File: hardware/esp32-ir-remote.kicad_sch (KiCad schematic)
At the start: 72 parts, among them J2 USB_C_Receptacle_USB2.0_14P, J3 Qwiic_I2C, J4 GPIO_PWR, J5 EXT_IR, J6 JTAG, Q1 Q_NPN_BCE, Q2 Q_NPN_BCE, Q3 IRLML6344, Q4 2N7002, Q5 2N7002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

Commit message: Fix BOM blockers found by adversarial LCSC validation (pre-routing)
Subagent validated all 35 LCSC codes against the live catalog; findings fixed:
- BLOCKER: Q1/Q2 used Q_NPN_BCE symbol but S8050 (C2146) SOT-23 is B-E-C -
  collector/emitter were swapped on the physical part (auto-reset would not
  work). Embedded symbol pin numbers swapped -> Q_NPN_BEC, wires untouched,
  netlist nodes confirm C: pad2->3, E: pad3->2; PCB pad nets swapped to match.
- BLOCKER: SW1/SW2 carried SMD switch code C455280 (TS-1088R 4x3mm) on a THT
  6mm footprint - unassemblable. Footprint -> JLC-MCP:SW-SMD_L3.9-W3.0-P4.45
  (fetched via jlcpcb MCP, validated 2 pads, clean layers); now SMT-line
  assemblable.
- HIGH: R9-R12+R30 carried C17955 = 20 ohm, not 18 - IR drive current 10% low.
  -> C17922 (18 ohm 1206 1% 250mW, Extended accepted: power margin per
  ir-transmitter.md needs 1206/0.25W).
- HIGH: 0805 codes on 1206 footprints: R3-R8+R22 -> C17902 (10k 1206 Basic);
  R1/R2 + R13/R16-R19 -> footprints to R_0805 keeping Basic 0805 codes
  (no Basic 1206 exists for 5.1k/470R).
- HIGH: JP1 testpoint (0.8mm drills) had pin-header code C124375 that cannot
  fit - code removed; JP1 is a solder-bridge/test-point, no part.
- Noted for order time: AM2302 stock critically low (37 units).

Verified: ERC 0 errors; netlist partition PCB==schematic identical;
footprint/value match 72/72; courtyard overlaps 0. BOM CSV regenerated.
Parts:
- JP1: LCSC C124375 -> (none)
- Q1, Q2: value Q_NPN_BCE -> Q_NPN_BEC; symbol Transistor_BJT:Q_NPN_BCE -> Transistor_BJT:Q_NPN_BEC
- R1, R13, R16, R17, R18, R19, R2: footprint Resistor_SMD:R_1206_3216Metric -> Resistor_SMD:R_0805_2012Metric
- R10, R11, R12, R30, R9: LCSC C17955 -> C17922
- R22, R3, R4, R5, R6, R7, R8: LCSC C17414 -> C17902
- SW1, SW2: footprint Button_Switch_THT:SW_PUSH_6mm -> JLC-MCP:SW-SMD_L3.9-W3.0-P4.45
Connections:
- net ESP_EN: now also Q1.3 (C); no longer Q1.2 (C)
- net ESP_GPIO0: now also Q2.3 (C); no longer Q2.2 (C)
- net at R21.1, R3.1: now also Q2.2 (E); no longer Q2.3 (E)
- net at R26.2, R4.2: now also Q1.2 (E); no longer Q1.3 (E)
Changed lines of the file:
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@@
 			(effects (font (size 1.27 1.27)) (hide yes))
 		)
-		(property "LCSC" "C17955"
+		(property "LCSC" "C17922"
 			(at 195.58 73.66 0)
 			(effects (font (size 1.27 1.27)) (hide yes))
@@
 			(effects (font (size 1.27 1.27)) (hide yes))
 		)
-		(property "LCSC" "C17414"
+		(property "LCSC" "C17902"
 			(at 179.07 115.57 0)
 			(effects (font (size 1.27 1.27)) (hide yes))
@@
 			(effects (font (size 1.27 1.27)) (hide yes))
 		)
-		(property "LCSC" "C124375"
+		(property "LCSC" ""
 			(at 113.03 100.33 0)
 			(effects (font (size 1.27 1.27)) (hide yes))
@@
 			(effects (font (size 1.27 1.27)))
 		)
-		(property "Footprint" "Resistor_SMD:R_1206_3216Metric"
+		(property "Footprint" "Resistor_SMD:R_0805_2012Metric"
 			(at 252.73 112.268 90)
 			(effects (font (size 1.27 1.27)) (hide yes))
@@
 			(effects (font (size 1.27 1.27)) (justify left))
 		)
-		(property "Footprint" "Resistor_SMD:R_1206_3216Metric"
+		(property "Footprint" "Resistor_SMD:R_0805_2012Metric"
 			(at 166.878 58.42 90)
 			(effects (font (size 1.27 1.27)) (hide yes))
@@
 			(effects (font (size 1.27 1.27)))
 		)
-		(property "Footprint" "Button_Switch_THT:SW_PUSH_6mm"
+		(property "Footprint" "JLC-MCP:SW-SMD_L3.9-W3.0-P4.45"
 			(at 259.08 148.59 0)
 			(effects (font (size 1.27 1.27)) (hide yes))
@@
 			(effects (font (size 1.27 1.27)) (hide yes))
 		)
-		(property "LCSC" "C17414"
+		(property "LCSC" "C17902"
 			(at 198.12 151.13 0)
 			(effects (font (size 1.27 1.27)) (hide yes))
@@
 	)
 	(symbol
-		(lib_id "Transistor_BJT:Q_NPN_BCE")
+		(lib_id "Transistor_BJT:Q_NPN_BEC")
 		(at 176.53 144.78 0)
 		(mirror x)
@@
 			(effects (font (size 1.27 1.27)) (justify left))
 		)
-		(property "Value" "Q_NPN_BCE"
+		(property "Value" "Q_NPN_BEC"
 			(at 181.61 143.5101 0)
 			(effects (font (size 1.27 1.27)) (justify left))
@@
 			(effects (font (size 1.27 1.27)))
 		)
-		(property "Footprint" "Resistor_SMD:R_1206_3216Metric"
+		(property "Footprint" "Resistor_SMD:R_0805_2012Metric"
 			(at 252.73 89.408 90)
 			(effects (font (size 1.27 1.27)) (hide yes))
@@
 			(effects (font (size 1.27 1.27)) (hide yes))
 		)
-		(property "LCSC" "C17414"
+		(property "LCSC" "C17902"
 			(at 163.83 144.78 0)
 			(effects (font (size 1.27 1.27)) (hide yes))
@@
 			(effects (font (size 1.27 1.27)))
 		)
-		(property "Footprint" "Button_Switch_THT:SW_PUSH_6mm"
+		(property "Footprint" "JLC-MCP:SW-SMD_L3.9-W3.0-P4.45"
 			(at 259.08 137.16 0)
 			(effects (font (size 1.27 1.27)) (hide yes))
@@
 			(effects (font (size 1.27 1.27)) (hide yes))
 		)
-		(property "LCSC" "C17414"
+		(property "LCSC" "C17902"
 			(at 87.63 49.53 0)
 			(effects (font (size 1.27 1.27)) (hide yes))
@@
 			(effects (font (size 1.27 1.27)))
 		)
-		(property "Footprint" "Resistor_SMD:R_1206_3216Metric"
+		(property "Footprint" "Resistor_SMD:R_0805_2012Metric"
 			(at 252.73 100.838 90)
 			(effects (font (size 1.27 1.27)) (hide yes))
@@
 			(effects (font (size 1.27 1.27)) (hide yes))
 		)
-		(property "LCSC" "C17955"
+		(property "LCSC" "C17922"
 			(at 195.58 50.8 0)
 			(effects (font (size 1.27 1.27)) (hide yes))
@@
 			(effects (font (size 1.27 1.27)) (hide yes))
 		)
-		(property "LCSC" "C17414"
+		(property "LCSC" "C17902"
 			(at 101.6 49.53 0)
 			(effects (font (size 1.27 1.27)) (hide yes))
@@
 			(effects (font (size 1.27 1.27)) (hide yes))
 		)
-		(property "LCSC" "C17955"
+		(property "LCSC" "C17922"
 			(at 195.58 62.23 0)
 			(effects (font (size 1.27 1.27)) (hide yes))
@@
 			(effects (font (size 1.27 1.27)) (justify left))
 		)
-		(property "Footprint" "Resistor_SMD:R_1206_3216Metric"
+		(property "Footprint" "Resistor_SMD:R_0805_2012Metric"
 			(at 165.862 48.26 90)
 			(effects (font (size 1.27 1.27)) (hide yes))
@@
 			(effects (font (size 1.27 1.27)))
 		)
-		(property "Footprint" "Resistor_SMD:R_1206_3216Metric"
+		(property "Footprint" "Resistor_SMD:R_0805_2012Metric"
 			(at 198.12 85.852 90)
 			(effects (font (size 1.27 1.27)) (hide yes))
@@
 			(effects (font (size 1.27 1.27)) (hide yes))
 		)
-		(property "LCSC" "C17955"
+		(property "LCSC" "C17922"
 			(at 195.58 39.37 0)
 			(effects (font (size 1.27 1.27)) (hide yes))
@@
 			(effects (font (size 1.27 1.27)) (hide yes))
 		)
-		(property "LCSC" "C17414"
+		(property "LCSC" "C17902"
 			(at 163.83 132.08 0)
 			(effects (font (size 1.27 1.27)) (hide yes))
@@
 			(effects (font (size 1.27 1.27)) (hide yes))
 		)
-		(property "LCSC" "C17414"
+		(property "LCSC" "C17902"
 			(at 161.29 168.91 0)
 			(effects (font (size 1.27 1.27)) (hide yes))
@@
 			(effects (font (size 1.27 1.27)))
 		)
-		(property "Footprint" "Resistor_SMD:R_1206_3216Metric"
+		(property "Footprint" "Resistor_SMD:R_0805_2012Metric"
 			(at 252.73 123.698 90)
 			(effects (font (size 1.27 1.27)) (hide yes))
@@
 	)
 	(symbol
-		(lib_id "Transistor_BJT:Q_NPN_BCE")
+		(lib_id "Transistor_BJT:Q_NPN_BEC")
 		(at 176.53 132.08 0)
 		(unit 1)
@@
 			(effects (font (size 1.27 1.27)) (justify left))
 		)
-		(property "Value" "Q_NPN_BCE"
+		(property "Value" "Q_NPN_BEC"
 			(at 181.61 133.3499 0)
 			(effects (font (size 1.27 1.27)) (justify left))
@@
 			(effects (font (size 1.27 1.27)) (hide yes))
 		)
-		(property "LCSC" "C17955"
+		(property "LCSC" "C17922"
 			(at 43.18 163.83 0)
 			(effects (font (size 1.27 1.27)) (hide yes))

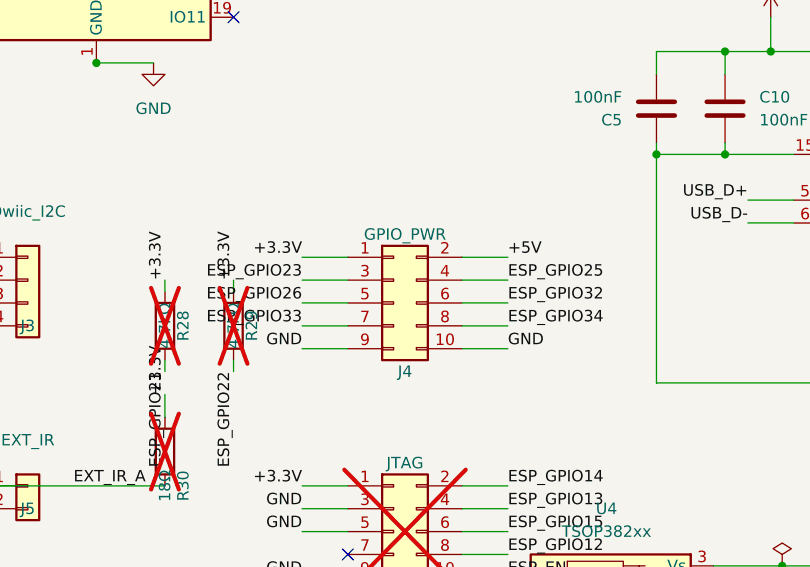
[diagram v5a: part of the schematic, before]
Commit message: H2.3: zero splits again - all nets connected (probed-lane hand routes)
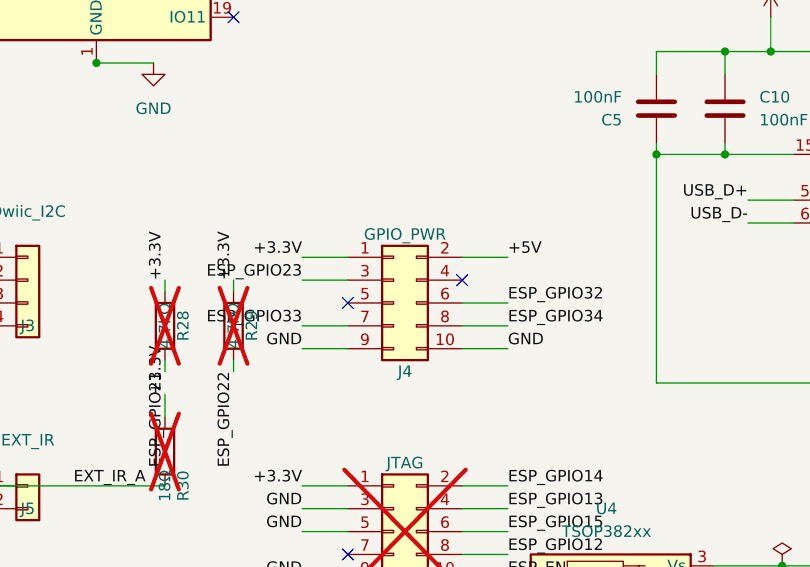
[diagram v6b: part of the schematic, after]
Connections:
- net ESP_GPIO25: no longer J4.4 (Pin_4)
- net ESP_GPIO26: no longer J4.5 (Pin_5)
- no-connect marks 16 -> 18
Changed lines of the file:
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@@
 		)
 	)
-	(sheet_instances (path "/" (page "1")))
+		(no_connect
+		(at 76.2 140.97)
+	)
+	(no_connect
+		(at 63.5 143.51)
+	)
+(sheet_instances (path "/" (page "1")))
 	(embedded_fonts no)
 	(no_connect
@@
 	)
 	(wire
-		(pts (xy 63.5 143.51) (xy 58.42 143.51))
-		(stroke (width 0) (type default))
-	)
-	(wire
 		(pts (xy 63.5 146.05) (xy 58.42 146.05))
 		(stroke (width 0) (type default))
@@
 	(wire
 		(pts (xy 76.2 138.43) (xy 81.28 138.43))
-		(stroke (width 0) (type default))
-	)
-	(wire
-		(pts (xy 76.2 140.97) (xy 81.28 140.97))
 		(stroke (width 0) (type default))
 	)
@@
 	(label "ESP_GPIO23"
 		(at 58.42 140.97 180)
-		(effects (font (size 1.27 1.27)) (justify right bottom))
-	)
-	(label "ESP_GPIO26"
-		(at 58.42 143.51 180)
 		(effects (font (size 1.27 1.27)) (justify right bottom))
 	)
@@
 		(effects (font (size 1.27 1.27)) (justify left bottom))
 	)
-	(label "ESP_GPIO25"
-		(at 81.28 140.97 0)
-		(effects (font (size 1.27 1.27)) (justify left bottom))
-	)

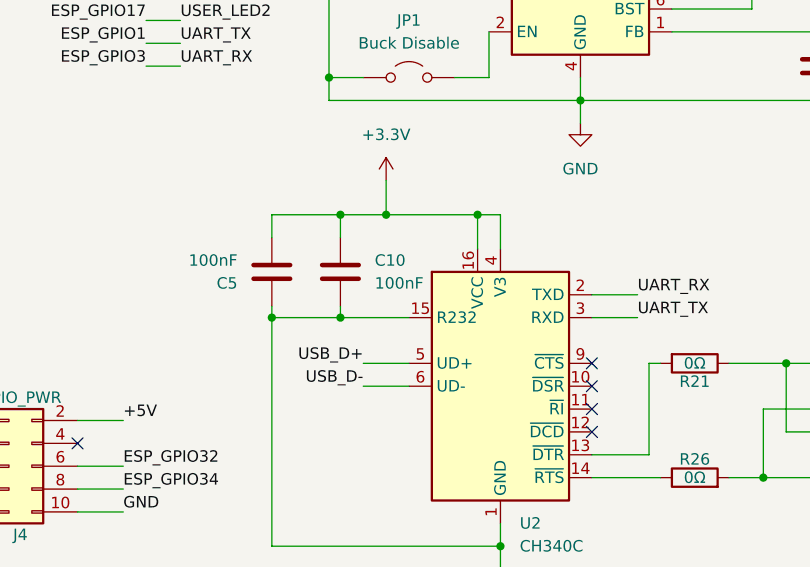
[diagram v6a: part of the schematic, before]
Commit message: H2.5 remediation complete: layout-review fixes verified, fab files re-exported
Review fixes (second pass after the H-1/H-2/M-1..M-4 rework broke nets):
- H-2: +3.3V/+5V/LED-anode nets widened 0.2->0.5 in place; DRC-driven
  selective neckdowns where lanes are tight (64 segs)
- H-1: SW-node direct route kept; 2 segs necked 0.6->0.5 for GND pad
  clearance
- M-1: buck B-keepout final extent (104.3,93.5)-(117.5,103.7); south edge
  set by the BST bootstrap B-jog (BST and JP1-B provably cross on F.Cu
  alone - see layout.md). pcb_finish.py learned BLOCK env to respect it.
- Repaired rework collateral: BST ripped-not-rehealed (bootstrap cap!),
  JP1-B corridor war (rip + hand BST jog + reroute), J5-move collisions
  (GPIO22/33/USER_LED2), 3 missing-via F/B gaps, +5V@J4 bbox-phantom gap,
  2 undersized healer vias (0.25 drill), ~100 dangling debris segs pruned,
  isolated stitch vias removed, C3/2 GND bond via + solid zone connection
- .kicad_pro: Power/IR_Drive netclasses restored (clobbered by a pcbnew
  save before last commit; netlist class column now matches again)

Final verification: DRC = 3 accepted errors (H1 antenna keepout pair +
H1/U3 courtyard) + 7 pour-fragment notices; zero real unconnected items;
schematic parity 0; ERC 0. Fab set re-exported (gerbers all drills >=0.3,
CPL delta = J5 move only), renders + GLB rebuilt.
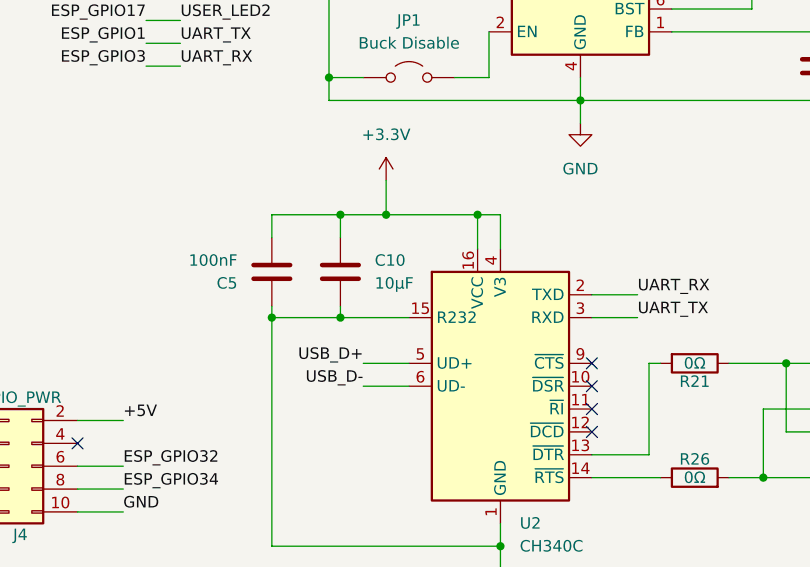
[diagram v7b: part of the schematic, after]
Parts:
- C10: value 100nF -> 10µF; LCSC C14663 -> C19702
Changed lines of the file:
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@@
 			(effects (font (size 1.27 1.27)) (justify left))
 		)
-		(property "Value" "100nF"
+		(property "Value" "10µF"
 			(at 109.22 123.1899 0)
 			(effects (font (size 1.27 1.27)) (justify left))
@@
 			(effects (font (size 1.27 1.27)) (hide yes))
 		)
-		(property "LCSC" "C14663"
+		(property "LCSC" "C19702"
 			(at 105.41 121.92 0)
 			(effects (font (size 1.27 1.27)) (hide yes))

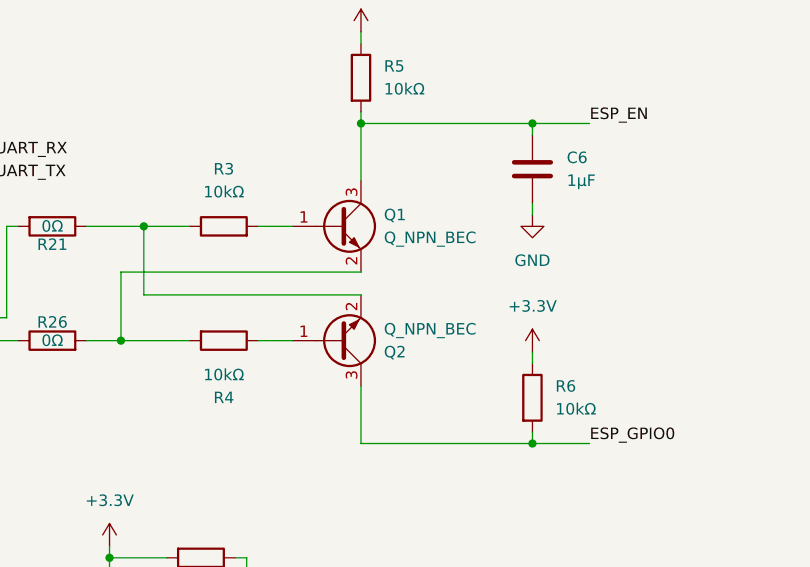
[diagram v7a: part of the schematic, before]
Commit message: Auto-reset Q1/Q2: S8050 NPN BJTs -> 2N7002 N-MOSFETs (board v1.3)
Swap the cross-coupled auto-reset transistors to the 2N7002 already used
at Q4/Q5. The SOT-23 pinouts map 1:1 (B->G, E->S, C->D on the same pads),
so the swap is layout-neutral: no copper, placement, or gerber changes.
Consolidates the BOM 35->34 unique lines (C2146 dropped; Q1/Q2/Q4/Q5 all
C8545, JLCPCB Basic, 779k stock).

Verified headlessly in kicad/kicad:9.0.6 (files also read clean under
10.0.2, the Pages CI image):
- ERC: -2 warnings (old Q1/Q2 lib_symbol_mismatch gone), no new
  violations; the 2 GPIO25/26 dangling-label errors pre-exist (J4
  deviation).
- Netlist diff electrically empty: same pads, same net partitions; only
  pin names and derived net names changed (Net-(Q1-B)->(Q1-G) etc.),
  renamed in the PCB to match.
- DRC unchanged vs accepted baseline (3 accepted errors, 7 pour
  notices); schematic parity 0; netlist<->PCB partition check identical.

Also fixes a latent fab bug found while regenerating the BOM: the
committed BOM CSV and fab BOM still ordered C10 as 100nF C14663, stale
vs the M-4 remediation (10uF 0603 C19702, Basic, verified in stock).

Trade-off (FET body diodes: RTS->EN / DTR->GPIO0 conduct only while
RESET/BOOT is held with the port idle; momentary, CH340-limited,
breakable via R21/R26) documented in notes/usb-serial.md and spec v1.3.

https://claude.ai/code/session_01NnkrUCiFVFngztSgzPXbfT
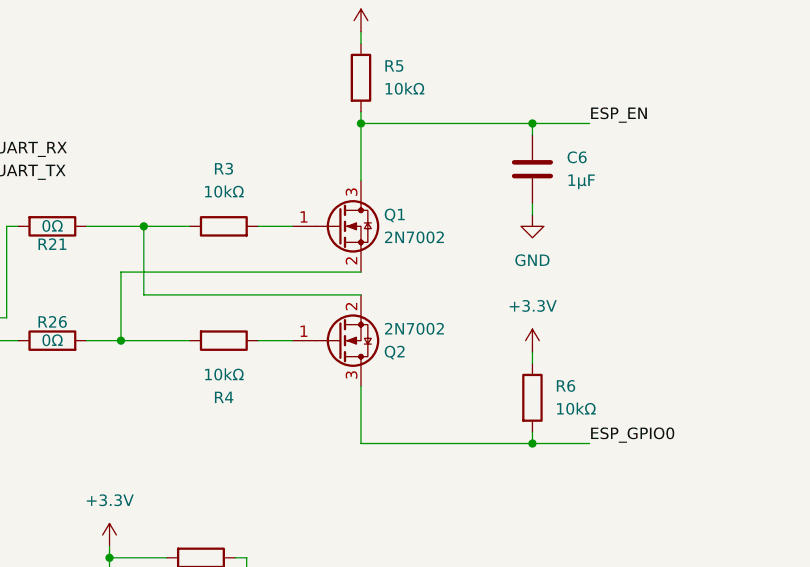
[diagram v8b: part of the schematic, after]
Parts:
- Q1, Q2: value Q_NPN_BEC -> 2N7002; symbol Transistor_BJT:Q_NPN_BEC -> Transistor_FET:Q_NMOS_GSD; LCSC C2146 -> C8545
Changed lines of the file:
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@@
 	)
 	(symbol
-		(lib_id "Transistor_BJT:Q_NPN_BEC")
+		(lib_id "Transistor_FET:Q_NMOS_GSD")
 		(at 176.53 144.78 0)
 		(mirror x)
@@
 			(effects (font (size 1.27 1.27)) (justify left))
 		)
-		(property "Value" "Q_NPN_BEC"
+		(property "Value" "2N7002"
 			(at 181.61 143.5101 0)
 			(effects (font (size 1.27 1.27)) (justify left))
@@
 			(effects (font (size 1.27 1.27)) (hide yes))
 		)
-		(property "Datasheet" "~"
+		(property "Datasheet" "https://www.lcsc.com/datasheet/lcsc_datasheet_2304140030_Jiangsu-Changjing-Electronics-Technology-Co---Ltd--2N7002_C8545.pdf"
 			(at 176.53 144.78 0)
 			(effects (font (size 1.27 1.27)) (hide yes))
 		)
-		(property "Description" "NPN transistor, base/collector/emitter"
+		(property "Description" "N-MOSFET transistor, gate/source/drain"
 			(at 176.53 144.78 0)
 			(effects (font (size 1.27 1.27)) (hide yes))
 		)
-		(property "LCSC" "C2146"
+		(property "LCSC" "C8545"
 			(at 176.53 144.78 0)
 			(effects (font (size 1.27 1.27)) (hide yes))
@@
 	)
 	(symbol
-		(lib_id "Transistor_BJT:Q_NPN_BEC")
+		(lib_id "Transistor_FET:Q_NMOS_GSD")
 		(at 176.53 132.08 0)
 		(unit 1)
@@
 			(effects (font (size 1.27 1.27)) (justify left))
 		)
-		(property "Value" "Q_NPN_BEC"
+		(property "Value" "2N7002"
 			(at 181.61 133.3499 0)
 			(effects (font (size 1.27 1.27)) (justify left))
@@
 			(effects (font (size 1.27 1.27)) (hide yes))
 		)
-		(property "Datasheet" "~"
+		(property "Datasheet" "https://www.lcsc.com/datasheet/lcsc_datasheet_2304140030_Jiangsu-Changjing-Electronics-Technology-Co---Ltd--2N7002_C8545.pdf"
 			(at 176.53 132.08 0)
 			(effects (font (size 1.27 1.27)) (hide yes))
 		)
-		(property "Description" "NPN transistor, base/collector/emitter"
+		(property "Description" "N-MOSFET transistor, gate/source/drain"
 			(at 176.53 132.08 0)
 			(effects (font (size 1.27 1.27)) (hide yes))
 		)
-		(property "LCSC" "C2146"
+		(property "LCSC" "C8545"
 			(at 176.53 132.08 0)
 			(effects (font (size 1.27 1.27)) (hide yes))
